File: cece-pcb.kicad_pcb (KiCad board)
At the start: 2 copper layers, 57 x 80.5 mm, 45 parts, among them J101 VAC, J102 HTU21D, J103 SERIAL, J104 Li-Ion Battery, K101 SANYOU_SRD_Form_C, Q101 Q_NPN, SW201 RES, U101 TLV75533PDBV, U102 MCP73811T-420I-OT, U201 ESP-12F

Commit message: Draft layout for the new HW revision (just for show)
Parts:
- added REF**: DFN-6-1EP_3x3mm_P1mm_EP1.5x2.4mm, Package_DFN_QFN:DFN-6-1EP_3x3mm_P1mm_EP1.5x2.4mm, F.Cu at (216.6, 81.5)
- added REF**: PinHeader_1x03_P2.54mm_Vertical, Connector_PinHeader_2.54mm:PinHeader_1x03_P2.54mm_Vertical, B.Cu at (205.7, 83.2)
- added REF**: PinHeader_1x02_P2.54mm_Horizontal, Connector_PinHeader_2.54mm:PinHeader_1x02_P2.54mm_Horizontal, B.Cu at (200.0, 47.0)
- added REF**: PinHeader_1x04_P2.54mm_Horizontal, Connector_PinHeader_2.54mm:PinHeader_1x04_P2.54mm_Horizontal, B.Cu at (212.7, 47.0)
- added REF**: SW_PUSH_6mm, Button_Switch_THT:SW_PUSH_6mm, F.Cu at (233.7, 80.6)
- added REF**: SW_PUSH_6mm, Button_Switch_THT:SW_PUSH_6mm, F.Cu at (233.7, 46.4)
- added REF**: ESP-07, RF_Module:ESP-07, F.Cu at (229.2, 60.9)
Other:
- board size 57 x 80.5 mm -> 141.5 x 80.5 mm

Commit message: Improve ACDC converter design to make it more robust
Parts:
- added C101: 100u, Capacitor_THT:CP_Radial_D6.3mm_P2.50mm, F.Cu at (258.7, -4.10)
- added C102: 1u, Capacitor_SMD:C_0805_2012Metric_Pad1.15x1.40mm_HandSolder, F.Cu at (268.7, -12.1)
- added D101: SMBJ5.0A, Diode_SMD:D_SMB_Handsoldering, F.Cu at (261.1, -10.8)
- added F101: 1A slow blow, Capacitor_THT:C_Disc_D8.0mm_W5.0mm_P5.00mm, F.Cu at (269.2, -16.9)
- added REF**: vimar_plana_3P, pol:vimar_plana_3P, F.Cu at (187.3, 85.5)
- added RV101: 10D561K, Capacitor_THT:C_Disc_D7.5mm_W5.0mm_P7.50mm, F.Cu at (257.7, -16.9)
- added VP101: VimarPlana, pol:vimar_plana_3P, F.Cu at (188.0, 29.4)
- moved REF** 41.4 mm to (203.2, 41.9)
- moved REF** 31.8 mm to (194.9, 73.4), turned to 270 degrees
- moved REF** 27.3 mm to (207.0, 73.4), turned to 270 degrees
- moved REF** 1.53 mm to (216.5, 80.0), turned to 180 degrees
- moved REF** 0.64 mm to (233.7, 47.0)
- moved REF** 0.63 mm to (233.7, 80.0)
- renumbered C101 to C103, D101 to D102, D102 to D103, D103 to D105, D105 to D106, R103 to R102, R104 to R103
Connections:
- PS101 pad 1: /ACL -> Net-(F101-Pad1)
- U101 pad 1: +BATT -> +5V
- U101 pad 3: +BATT -> +5V
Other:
- board size 141.5 x 80.5 mm -> 141.6 x 80.5 mm
- board text added: "VIMAR PLANA 1P"

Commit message: Start defining PCB
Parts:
- removed the C102 at (268.7, -12.1)
- removed the C102 at (124.0, 72.6)
- removed the C103 at (140.2, 72.6)
- removed the C103 at (146.1, 65.0)
- removed C203: 1u, Capacitor_THT:C_Radial_D6.3mm_H5.0mm_P2.50mm
- removed C204: 100nF, Capacitor_THT:C_Disc_D4.3mm_W1.9mm_P5.00mm
- removed D103, D105: LED, LED_THT:LED_D3.0mm
- removed D104: Schottky SOT-23, Diode_SMD:D_SOT-23_ANK
- removed D106: Schottky SOD-123, Diode_SMD:D_SOD-123F
- removed F101: 1A slow blow, Capacitor_THT:C_Disc_D8.0mm_W5.0mm_P5.00mm
- removed H101, H102, H103, H104: MountingHole_Pad, MountingHole:MountingHole_3.2mm_M3_Pad
- removed J104: Li-Ion Battery, Connector_PinHeader_2.54mm:PinHeader_1x02_P2.54mm_Vertical
- removed JP201: PROG, Connector_PinHeader_2.54mm:PinHeader_1x02_P2.54mm_Vertical
- removed JP202: Deep_Sleep, Jumper:SolderJumper-2_P1.3mm_Open_Pad1.0x1.5mm
- removed K101: SANYOU_SRD_Form_C, Relay_THT:Relay_SPDT_SANYOU_SRD_Series_Form_C
- removed PS101: HLK-PM01, Converter_ACDC:Converter_ACDC_HiLink_HLK-PMxx
- removed Q101: Q_NPN, Package_TO_SOT_THT:TO-92L_Inline_Wide
- removed R203, R204, R206: 10k, Resistor_THT:R_Axial_DIN0207_L6.3mm_D2.5mm_P7.62mm_Horizontal
- removed R205: 220k, Resistor_THT:R_Axial_DIN0207_L6.3mm_D2.5mm_P7.62mm_Horizontal
- removed R207: 100k, Resistor_THT:R_Axial_DIN0207_L6.3mm_D2.5mm_P7.62mm_Horizontal
- removed R208: 100, Resistor_THT:R_Axial_DIN0207_L6.3mm_D2.5mm_P7.62mm_Horizontal
- removed REF**: vimar_plana_3P, pol:vimar_plana_3P
- removed REF**: DFN-6-1EP_3x3mm_P1mm_EP1.5x2.4mm, Package_DFN_QFN:DFN-6-1EP_3x3mm_P1mm_EP1.5x2.4mm
- removed REF**: PinHeader_1x03_P2.54mm_Vertical, Connector_PinHeader_2.54mm:PinHeader_1x03_P2.54mm_Vertical
- removed REF**: PinHeader_1x02_P2.54mm_Horizontal, Connector_PinHeader_2.54mm:PinHeader_1x02_P2.54mm_Horizontal
- removed REF**: PinHeader_1x04_P2.54mm_Horizontal, Connector_PinHeader_2.54mm:PinHeader_1x04_P2.54mm_Horizontal
- removed REF** (x2): SW_PUSH_6mm, Button_Switch_THT:SW_PUSH_6mm
- removed REF**: ESP-07, RF_Module:ESP-07
- removed RV101: 10D561K, Capacitor_THT:C_Disc_D7.5mm_W5.0mm_P7.50mm
- removed SW201: RES, Button_Switch_THT:SW_PUSH_6mm
- removed U201: ESP-12F, ESP8266:ESP-12E
- added C102: 10u, Capacitor_SMD:C_0805_2012Metric_Pad1.15x1.40mm_HandSolder, F.Cu at (133.9, 0.10)
- added C103: 1u, Capacitor_SMD:C_0805_2012Metric_Pad1.15x1.40mm_HandSolder, F.Cu at (111.7, 13.3)
- added C104: 100nF, Capacitor_SMD:C_0805_2012Metric_Pad1.15x1.40mm_HandSolder, F.Cu at (110.9, -4.70)
- added C105: 100p, Capacitor_SMD:C_0805_2012Metric_Pad1.15x1.40mm_HandSolder, F.Cu at (125.8, -0.15)
- added C106: 100p, Capacitor_SMD:C_0805_2012Metric_Pad1.15x1.40mm_HandSolder, F.Cu at (121.3, 2.80)
- added C107: 100nF, Capacitor_SMD:C_0805_2012Metric_Pad1.15x1.40mm_HandSolder, F.Cu at (121.7, -12.2)
- added C108: 100nF, Capacitor_SMD:C_0805_2012Metric_Pad1.15x1.40mm_HandSolder, F.Cu at (123.5, 7.80)
- added D201: 1N4001, Diode_THT:D_DO-41_SOD81_P7.62mm_Horizontal, B.Cu at (158.1, 90.8)
- added D202: LED, LED_THT:LED_D3.0mm, F.Cu at (147.3, 81.3)
- added D203: SMBJ5.0A, Diode_SMD:D_SMB_Handsoldering, B.Cu at (131.4, 83.2)
- added EA201: a_black_cat, pol:a_black_cat, F.Cu at (106.0, 85.7)
- added F201: 1A slow blow, Capacitor_THT:C_Disc_D8.0mm_W5.0mm_P5.00mm, B.Cu at (113.5, 111.1)
- added FB101: Ferrite_Bead, Resistor_SMD:R_0805_2012Metric_Pad1.15x1.40mm_HandSolder, F.Cu at (116.5, 4.70)
- added J201: VAC, TerminalBlock:TerminalBlock_bornier-5_P5.08mm, F.Cu at (104.8, 90.8)
- added J202: Conn_01x03_Female, Connector_PinHeader_2.54mm:PinHeader_1x03_P2.54mm_Vertical, B.Cu at (113.4, 72.9)
- added K201: SANYOU_SRD_Form_C, Relay_THT:Relay_SPDT_SANYOU_SRD_Series_Form_C, F.Cu at (154.3, 94.6)
- added PS201: HLK-PM01, Converter_ACDC:Converter_ACDC_HiLink_HLK-PMxx, F.Cu at (128.9, 111.1)
- added Q201: Q_NPN, Package_TO_SOT_THT:TO-92L_Inline_Wide, B.Cu at (147.3, 85.7)
- added R104: 10k, Resistor_SMD:R_0805_2012Metric_Pad1.15x1.40mm_HandSolder, F.Cu at (116.3, -1.20)
- added R106: 10k, Resistor_SMD:R_0805_2012Metric_Pad1.15x1.40mm_HandSolder, F.Cu at (110.9, -11.9)
- added R107: 330, Resistor_SMD:R_0805_2012Metric_Pad1.15x1.40mm_HandSolder, F.Cu at (116.5, 7.65)
- added RV201: 10D561K, Capacitor_THT:C_Disc_D7.5mm_W5.0mm_P7.50mm, B.Cu at (119.4, 111.1)
- added SW101: SW_Push, Button_Switch_THT:SW_PUSH_6mm, F.Cu at (140.0, 31.5)
- added SW102: SW_Push, Button_Switch_THT:SW_PUSH_6mm, F.Cu at (133.5, 59.4)
- added U103: LM75C, Package_SO:SOIC-8_3.9x4.9mm_P1.27mm, F.Cu at (126.5, 27.7)
- C101: value 100u -> 1u; footprint Capacitor_THT:CP_Radial_D6.3mm_P2.50mm -> Capacitor_SMD:C_0805_2012Metric_Pad1.15x1.40mm_HandSolder
- C201: value 100nF -> 10u; footprint Capacitor_THT:C_Disc_D4.3mm_W1.9mm_P5.00mm -> Capacitor_THT:C_Radial_D6.3mm_H5.0mm_P2.50mm
- C202: value 10u -> 100u; footprint Capacitor_THT:C_Radial_D6.3mm_H5.0mm_P2.50mm -> Capacitor_THT:CP_Radial_D6.3mm_P2.50mm
- D101: value SMBJ5.0A -> Schottky SOT-23; footprint Diode_SMD:D_SMB_Handsoldering -> Diode_SMD:D_SOT-23_ANK
- D102: value 1N4001 -> Schottky SOD-123; footprint Diode_THT:D_DO-41_SOD81_P7.62mm_Horizontal -> Diode_SMD:D_SOD-123F
- J101: value VAC -> SERIAL; footprint TerminalBlock:TerminalBlock_bornier-5_P5.08mm -> Connector_PinHeader_2.54mm:PinHeader_1x04_P2.54mm_Vertical
- J103: value SERIAL -> Conn_01x03_Male; footprint Connector_PinHeader_2.54mm:PinHeader_1x04_P2.54mm_Vertical -> Connector_PinSocket_2.54mm:PinSocket_1x03_P2.54mm_Vertical; moved to B.Cu
- JP101: value VBATT_A0 -> RST; footprint Jumper:SolderJumper-2_P1.3mm_Bridged_Pad1.0x1.5mm -> Connector_PinHeader_2.54mm:PinHeader_1x02_P2.54mm_Vertical
- JP102: value VBATT 5V -> PROG; footprint Jumper:SolderJumper-2_P1.3mm_Open_Pad1.0x1.5mm -> Connector_PinHeader_2.54mm:PinHeader_1x02_P2.54mm_Vertical
- JP103: value 73811 -> Deep_Sleep; moved to F.Cu
- R101: value 220 -> 10k; footprint Resistor_THT:R_Axial_DIN0207_L6.3mm_D2.5mm_P7.62mm_Horizontal -> Resistor_SMD:R_0805_2012Metric_Pad1.15x1.40mm_HandSolder
- R102: value 1k -> 10k; footprint Resistor_THT:R_Axial_DIN0207_L6.3mm_D2.5mm_P7.62mm_Horizontal -> Resistor_SMD:R_0805_2012Metric_Pad1.15x1.40mm_HandSolder
- R103: value 100 -> 10k; footprint Resistor_THT:R_Axial_DIN0207_L6.3mm_D2.5mm_P7.62mm_Horizontal -> Resistor_SMD:R_0805_2012Metric_Pad1.15x1.40mm_HandSolder
- R105: value R_PROG -> 330; moved to F.Cu
- R201: value 10k -> 220; moved to B.Cu
- R202: value 10k -> 1k; moved to B.Cu
- U101: moved to B.Cu
- U102: value MCP73811T-420I-OT -> ESP-12F/ESP07; footprint Package_TO_SOT_SMD:SOT-23-5 -> RF_Module:ESP-07; moved to F.Cu
- moved D101 150.3 mm to (116.5, 30.0), turned to 90 degrees
- moved C101 128.6 mm to (130.1, -3.50)
- moved VP101 96.9 mm to (100.0, 70.0)
- moved R103 93.8 mm to (116.3, 1.75), turned to 0 degrees
- moved J102 89.9 mm to (87.0, 23.0)
- moved R102 88.4 mm to (124.5, -6.05), turned to 0 degrees
- moved R105 79.7 mm to (124.5, -9.00), turned to 0 degrees
- moved R101 75.5 mm to (111.7, 10.3), turned to 0 degrees
- moved JP101 70.0 mm to (148.0, 25.5)
- moved JP103 60.2 mm to (111.5, 16.6), turned to 0 degrees
- moved J101 58.3 mm to (108.5, 26.5), turned to 90 degrees
- moved JP102 55.4 mm to (103.0, 29.0), turned to 180 degrees
- moved D102 47.8 mm to (120.0, 30.0), turned to 270 degrees
- moved R202 45.9 mm to (118.1, 76.8), turned to 180 degrees
- moved EA101 41.2 mm to (153.2, 25.9)
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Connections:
- C201 pad 1: /ESP-12_common/RST -> +5V
- C201 pad 2: Net-(C201-Pad2) -> GND
- C202 pad 1: +3V3 -> +5V
- D101 pad 1: +5V -> Net-(D101-Pad1)
- D101 pad 2: GND -> +3V3
- D102 pad 1: +BATT -> Net-(D101-Pad1)
- D102 pad 2: Net-(D102-Pad2) -> +3V3
- J101 pad 1: /NO -> GND
- J101 pad 2: /C -> Net-(J101-Pad2)
- J101 pad 3: /NC -> Net-(C106-Pad1)
- J101 pad 4: /ACN -> Net-(D101-Pad1)
- J102 pad 3: /HTU_SDA -> /D2|SDA
- J102 pad 4: /HTU_SCL -> /D1|SCL
- J103 pad 1: Net-(D104-Pad2) -> GND
- J103 pad 2: /RX -> /D8
- J103 pad 3: /TX -> +5V
- JP101 pad 1: +BATT -> /RST
- JP101 pad 2: /ESP-12_common/A0 -> GND
- JP102 pad 1: +5V -> /D3
- JP102 pad 2: +BATT -> GND
- JP103 pad 1: +5V -> /RST
- JP103 pad 2: Net-(JP103-Pad2) -> /D0
- R101 pad 1: Net-(D103-Pad2) -> /EN
- R101 pad 2: +BATT -> +3V3
- R102 pad 1: Net-(Q101-Pad2) -> /RST
- R102 pad 2: /RLY -> +3V3
- R103 pad 1: /ESP-12_common/D8 -> /D3
- R103 pad 2: Net-(D105-Pad2) -> +3V3
- R105 pad 1: Net-(JP103-Pad2) -> Net-(C106-Pad1)
- R105 pad 2: GND -> /TX
- R201 pad 1: +3V3 -> Net-(D202-Pad2)
- R201 pad 2: /ESP-12_common/RST -> +5V
- R202 pad 1: /ESP-12_common/EN -> Net-(Q201-Pad2)
- R202 pad 2: +3V3 -> /D8
- U101 pad 4: Net-(U101-Pad4) -> (no net)
- U102 pad 1: +5V -> /RST
- U102 pad 2: GND -> (no net)
- U102 pad 3: +BATT -> /EN
- U102 pad 4: +5V -> /D0
- U102 pad 5: Net-(JP103-Pad2) -> /D5|SCK
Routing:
- net +BATT: track 91.6 -> 0.00 mm
- net +3V3: track 75.5 -> 0.00 mm
- net /Bottom Board/NC: track 0.00 -> 63.8 mm
- net /Bottom Board/C: track 0.00 -> 59.3 mm
- net +5V: track 32.3 -> 90.4 mm, vias 3 -> 0
- net /RLY: track 48.8 -> 0.00 mm, vias 2 -> 0
- net /Bottom Board/NO: track 0.00 -> 48.3 mm
- net /ESP-12_common/RST: track 46.9 -> 0.00 mm, vias 2 -> 0
- net Net-(Q201-Pad2): track 0.00 -> 42.2 mm
- net /Bottom Board/ACN: track 0.00 -> 35.1 mm
- net /RX: track 33.8 -> 0.00 mm, vias 2 -> 0
- net /TX: track 31.4 -> 0.00 mm, vias 2 -> 0
- net /ACN: track 28.3 -> 0.00 mm
- net /C: track 26.1 -> 0.00 mm
- net Net-(D102-Pad2): track 21.9 -> 0.00 mm
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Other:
- board size 141.6 x 80.5 mm -> 67.3 x 93.8 mm
- net class Default: trace_width 0.127 -> 0.254
- rule trace_min: 0.127 -> 0.254
- board text removed: "*"
- board text removed: "+"
- board text removed: "3V3"
- board text removed: "<3V3"
- board text removed: "<A0"
- board text removed: "<D1"
- board text removed: "<D2"
- board text removed: "<D3"
- board text removed: "<D4"
- board text removed: "<D8"
- board text removed: "<RX"
- board text removed: "<TX"
- board text removed: "C"
- board text removed: "CECE r1.0"
- board text removed: "D0>"
- board text removed: "D5>"
- board text removed: "D6>"
- board text removed: "D7>"
- board text removed: "GND"
- board text removed: "L"
- board text removed: "N"
- board text removed: "NC"
- board text removed: "NO"
- board text removed: "RX"
- board text removed: "TX"

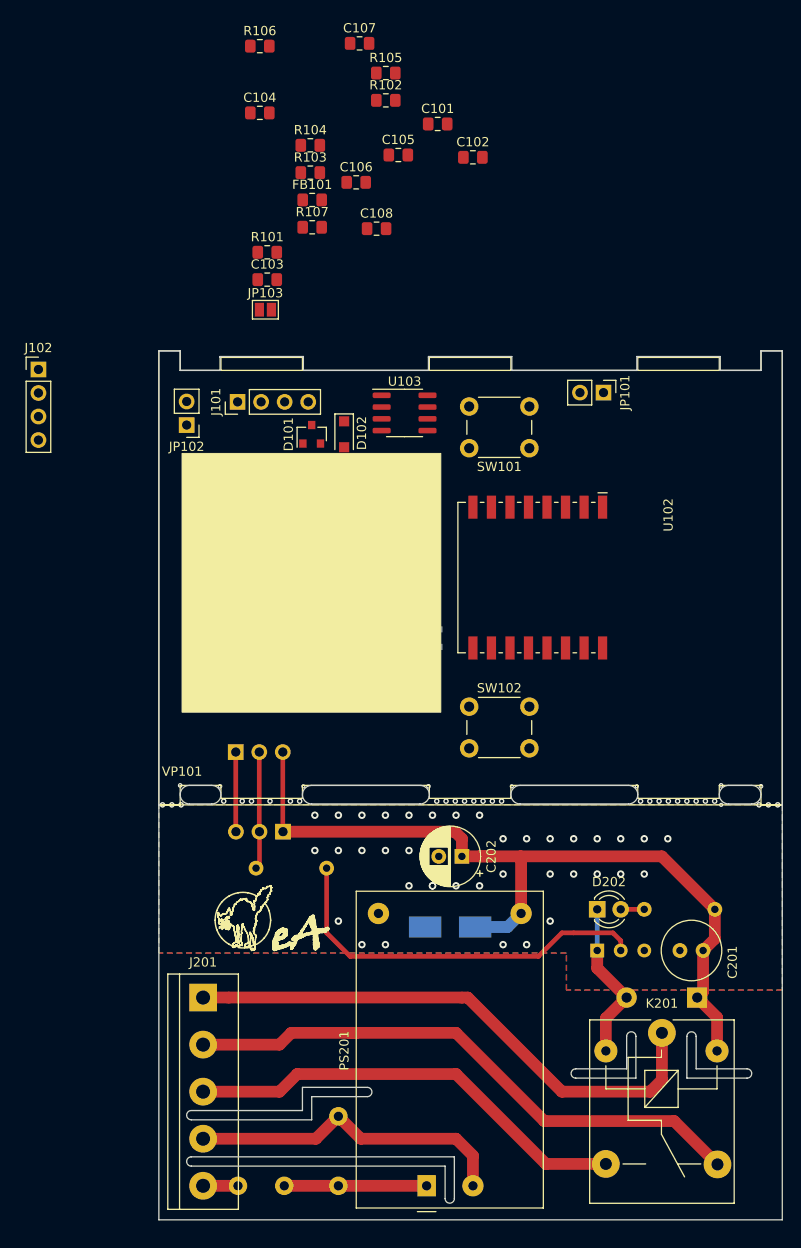
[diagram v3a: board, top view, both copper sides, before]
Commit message: Complete the PCB ready for final review
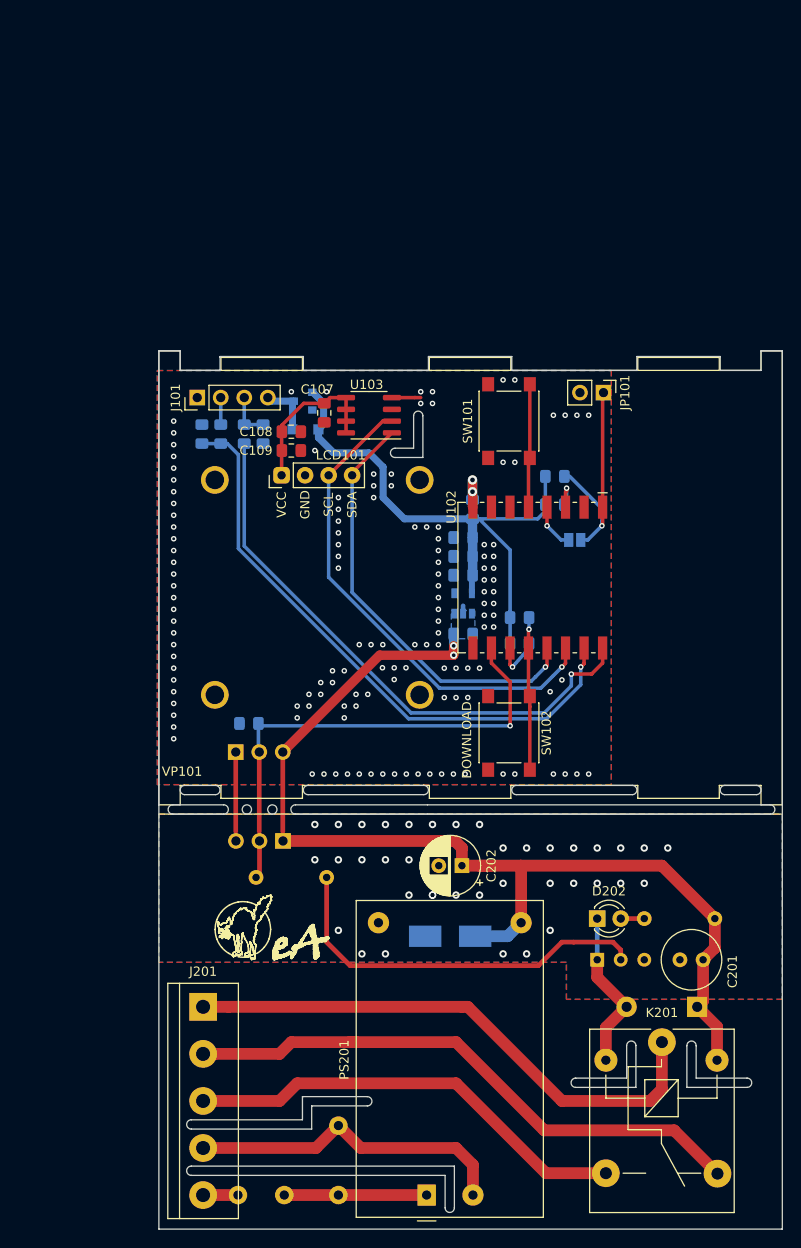
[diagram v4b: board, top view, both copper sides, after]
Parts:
- removed J102: HTU21D, Connector_PinHeader_2.54mm:PinHeader_1x04_P2.54mm_Vertical
- removed JP102: PROG, Connector_PinHeader_2.54mm:PinHeader_1x02_P2.54mm_Vertical
- added C109: 100nF, Capacitor_SMD:C_0805_2012Metric_Pad1.15x1.40mm_HandSolder, F.Cu at (114.3, 31.8)
- added LCD101: I2C_LCD_display, pol:I2C_LCD_display_0.96, F.Cu at (113.2, 34.4)
- C101, C102, C103, C104, C105, C106, D101, D102, FB101, JP103, R101, R102, R103, R104, R105, R106, R107: moved to B.Cu
- C108: value 100nF -> 10u
- SW101, SW102: footprint Button_Switch_THT:SW_PUSH_6mm -> Button_Switch_SMD:SW_Push_1P1T_NO_6x6mm_H9.5mm
- moved R106 73.1 mm to (109.7, 61.2)
- moved R104 58.3 mm to (138.9, 52.6), turned to 180 degrees
- moved C101 55.1 mm to (132.9, 51.6)
- moved R103 53.1 mm to (138.9, 49.8), turned to 180 degrees
- moved C104 50.8 mm to (132.8, 41.1), turned to 180 degrees
- moved C102 45.1 mm to (132.8, 45.2), turned to 180 degrees
- moved R102 44.5 mm to (142.7, 34.5), turned to 180 degrees
- moved R105 41.9 mm to (109.2, 30.0), turned to 270 degrees
- moved JP103 41.6 mm to (144.9, 41.4), turned to 180 degrees
- moved R101 41.3 mm to (142.7, 37.6), turned to 180 degrees
- moved C107 40.1 mm to (117.9, 27.7), turned to 270 degrees
- moved FB101 37.6 mm to (133.9, 38.1), turned to 270 degrees
- moved C105 36.8 mm to (104.6, 30.0), turned to 90 degrees
- moved C103 36.6 mm to (132.8, 43.2), turned to 180 degrees
- moved C106 29.0 mm to (111.3, 30.0), turned to 270 degrees
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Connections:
- C107 pad 1: (no net) -> +3V3
- C107 pad 2: (no net) -> GND
- C108 pad 1: (no net) -> +3V3
- C108 pad 2: (no net) -> GND
- SW102 pad 1: /D4 -> /D3
- U103 pad 4: (no net) -> GND
- U103 pad 5: (no net) -> +3V3
- U103 pad 6: (no net) -> +3V3
- U103 pad 7: (no net) -> +3V3
- U103 pad 8: (no net) -> +3V3
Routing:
- net +3V3: track 0.00 -> 80.8 mm
- net /RX: track 0.00 -> 64.8 mm, vias 0 -> 1
- net /TX: track 0.00 -> 61.8 mm, vias 0 -> 1
- net /D1|SCL: track 0.00 -> 53.6 mm, vias 0 -> 1
- net /D2|SDA: track 0.00 -> 46.6 mm, vias 0 -> 1
- net /D8: track 12.7 -> 52.3 mm, vias 0 -> 1
- net +5V: track 90.4 -> 116.5 mm, vias 0 -> 2
- net /RST: track 0.00 -> 24.7 mm, vias 0 -> 1
- net /D3: track 0.00 -> 17.0 mm, vias 0 -> 1
- net /D5|SCK: track 0.00 -> 13.3 mm
- net Net-(D101-Pad1): track 0.00 -> 6.08 mm
- net /D4: track 0.00 -> 5.38 mm, vias 0 -> 1
- net GND: track 8.61 -> 13.9 mm, vias 45 -> 174
- net /D0: track 0.00 -> 4.98 mm, vias 0 -> 1
- net Net-(FB101-Pad1): track 0.00 -> 4.98 mm, vias 0 -> 2
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- added copper zone on B.Cu, net +5V
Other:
- board size 67.3 x 93.8 mm -> 67.3 x 94.8 mm
- board text added: "DOWNLOAD"
- board text added: "Flip this way"
